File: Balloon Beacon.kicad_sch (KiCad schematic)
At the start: 52 parts, among them J1 PV Input, J2 Serial, J3 ICSP, J4 I2C, J6 GPS_ANT, Q1 AO3401A, U1 CJ431, U2 ATmega328PB-MU, U3 STC22K33048-26.000MT, U4 LM50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

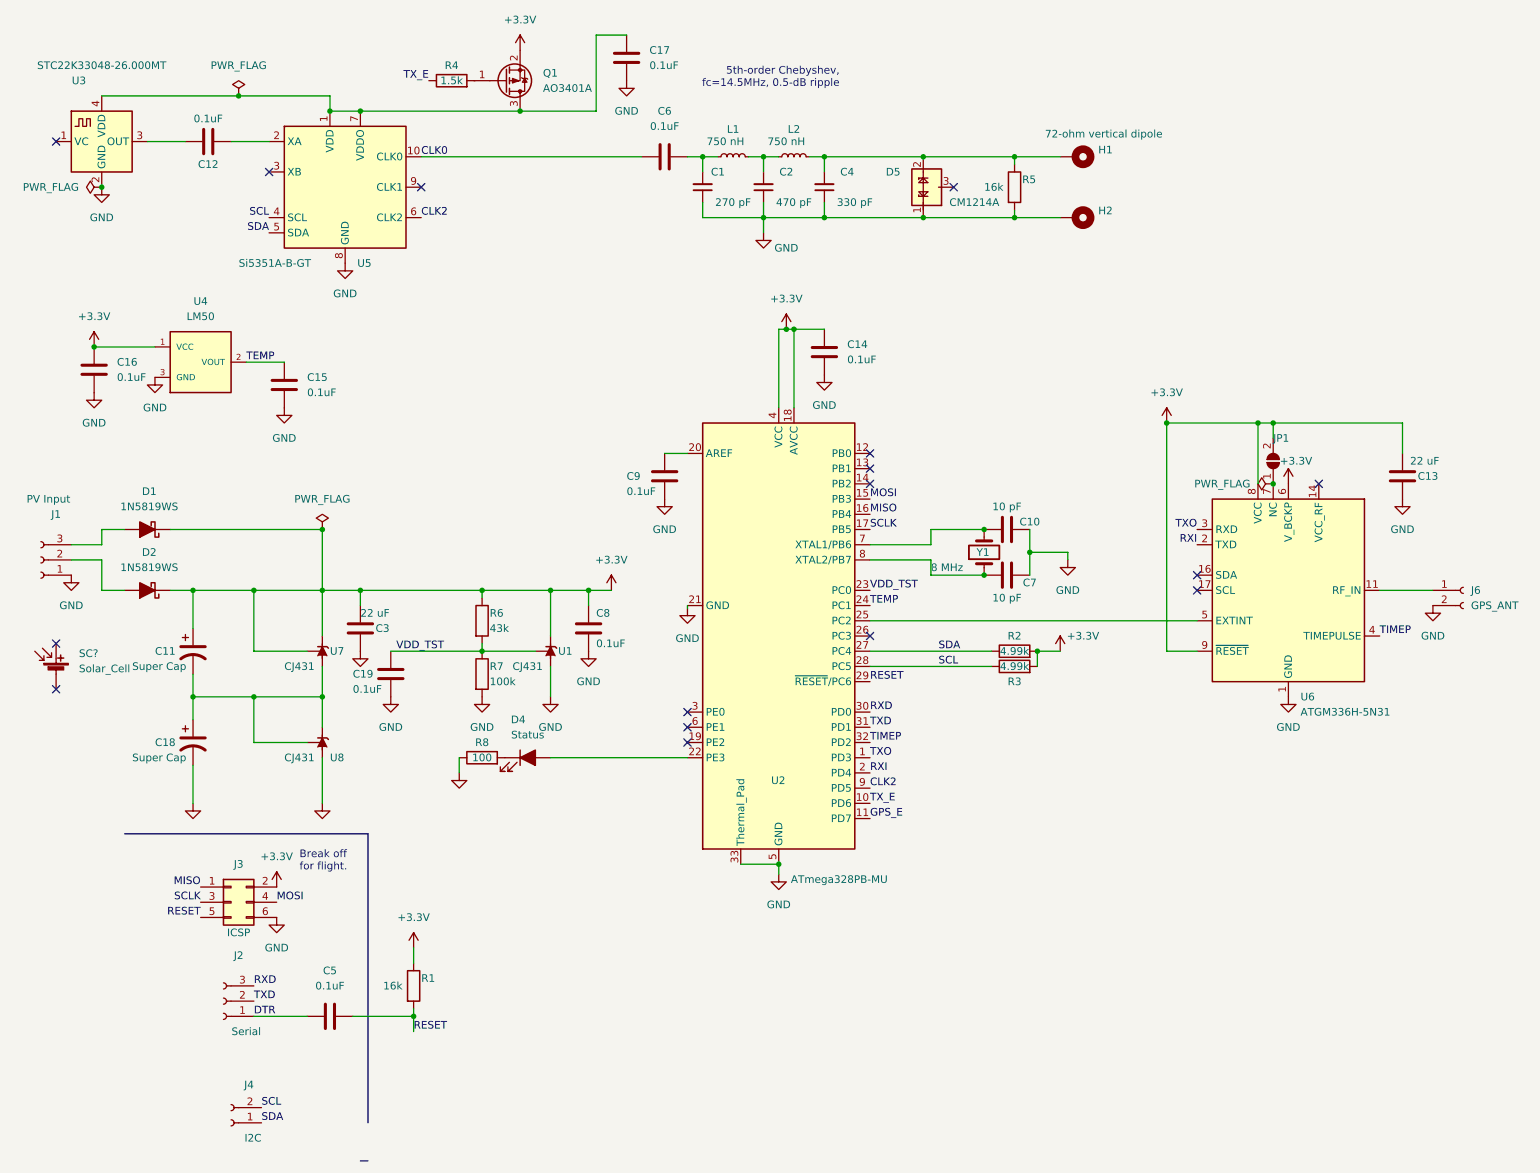
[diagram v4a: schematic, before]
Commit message: Changed TCXO to an available one.
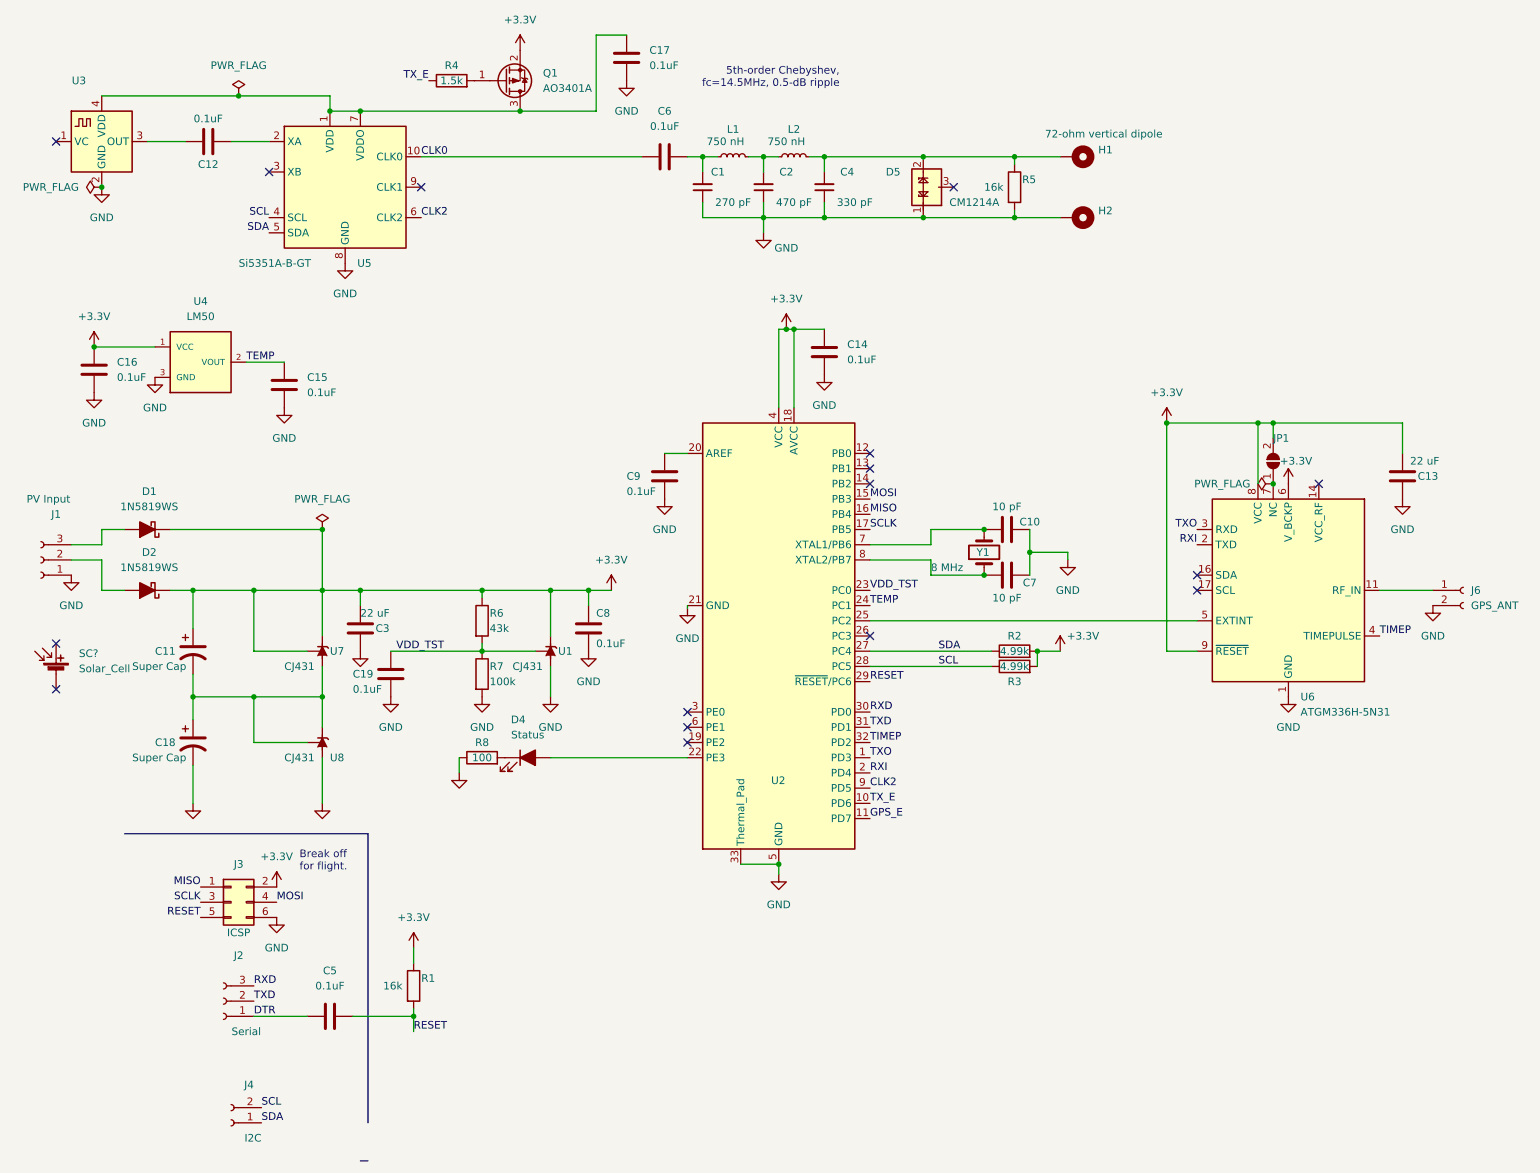
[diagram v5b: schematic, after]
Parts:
- U2: value ATmega328PB-MU -> (none); footprint Package_DFN_QFN:QFN-32-1EP_5x5mm_P0.5mm_EP3.3x3.3mm -> (none); LCSC C967933 -> (none)
- U3: value STC22K33048-26.000MT -> (none); footprint Oscillator:Oscillator_SMD_Fox_FT5H_5.0x3.2mm -> (none)
- U6: LCSC (none) -> C90770
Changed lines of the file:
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@@
       (effects (font (size 1.27 1.27)) (justify left))
     )
-    (property "Value" "ATmega328PB-MU" (id 1) (at 142.9894 157.48 0)
-      (effects (font (size 1.27 1.27)) (justify left))
-    )
-    (property "Footprint" "Package_DFN_QFN:QFN-32-1EP_5x5mm_P0.5mm_EP3.3x3.3mm" (id 2) (at 140.97 116.84 0)
+    (property "Value" "" (id 1) (at 142.9894 157.48 0)
+      (effects (font (size 1.27 1.27)) (justify left))
+    )
+    (property "Footprint" "" (id 2) (at 140.97 116.84 0)
       (effects (font (size 1.27 1.27) italic) hide)
     )
     (property "Datasheet" "http://ww1.microchip.com/downloads/en/DeviceDoc/40001906C.pdf" (id 3) (at 140.97 116.84 0)
-      (effects (font (size 1.27 1.27)) hide)
-    )
-    (property "LCSC" "C967933" (id 4) (at 140.97 116.84 0)
       (effects (font (size 1.27 1.27)) hide)
     )
@@
       (effects (font (size 1.27 1.27)) hide)
     )
+    (property "LCSC" "C90770" (id 4) (at 226.06 109.22 0)
+      (effects (font (size 1.27 1.27)) hide)
+    )
     (pin "1")
     (pin "10")
@@
     (in_bom yes) (on_board yes)
     (property "Reference" "U3" (id 0) (at 24.13 24.13 0))
-    (property "Value" "STC22K33048-26.000MT" (id 1) (at 27.94 21.59 0))
-    (property "Footprint" "Oscillator:Oscillator_SMD_Fox_FT5H_5.0x3.2mm" (id 2) (at 27.94 53.34 0)
-      (effects (font (size 1.27 1.27)) hide)
-    )
-    (property "Datasheet" "https://suntsu.com/wp-content/uploads/2019/07/STC22K-Series.pdf" (id 3) (at 27.94 34.29 0)
+    (property "Value" "" (id 1) (at 27.94 21.59 0))
+    (property "Footprint" "" (id 2) (at 27.94 53.34 0)
+      (effects (font (size 1.27 1.27)) hide)
+    )
+    (property "Datasheet" "https://www.taitien.com/wp-content/uploads/2015/12/XO-0076_TX.pdf" (id 3) (at 27.94 34.29 0)
       (effects (font (size 1.27 1.27)) hide)
     )
@@
     )
     (path "/ea8a827f-ae0c-4cf1-8927-35f036a4c0c6"
-      (reference "U3") (unit 1) (value "STC22K33048-26.000MT") (footprint "Oscillator:Oscillator_SMD_Fox_FT5H_5.0x3.2mm")
+      (reference "U3") (unit 1) (value "TXEABLSANF-24.000000") (footprint "Oscillator:Oscillator_SMD_EuroQuartz_XO32-4Pin_3.2x2.5mm_HandSoldering")
     )
     (path "/56d74f4a-c28a-4ee6-9f0c-d886e3d08c1f"

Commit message: Deleted a solar cell on the schematic.
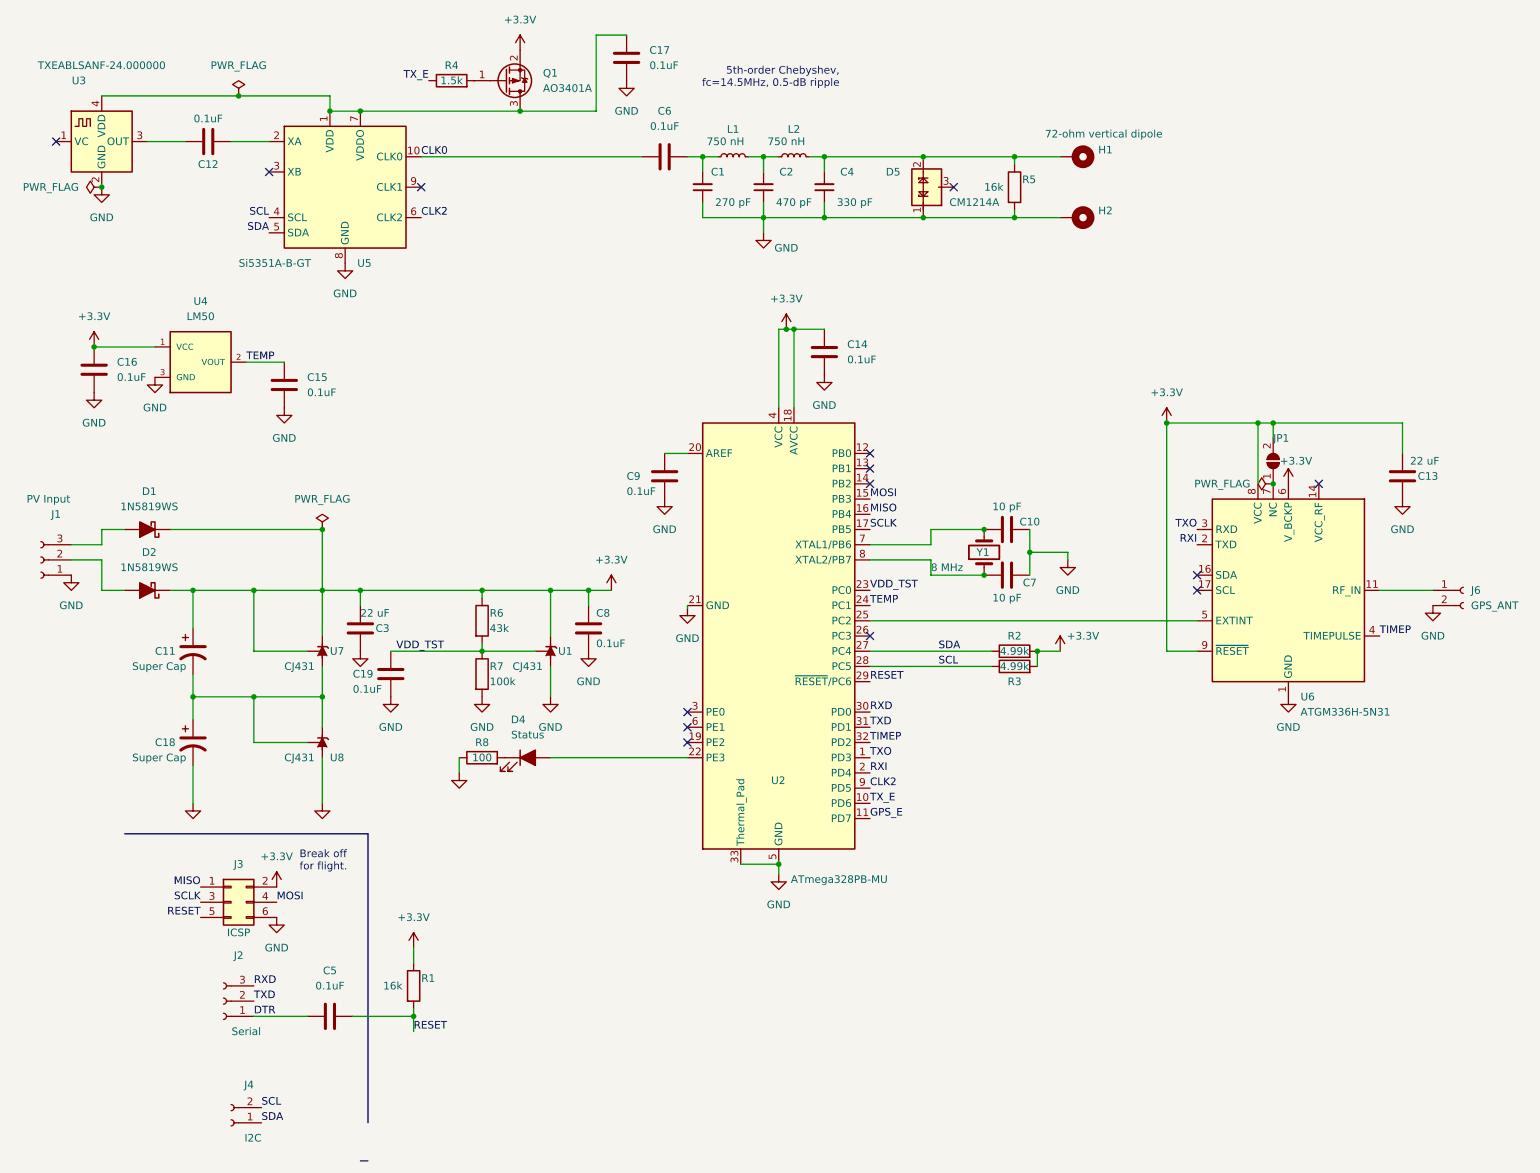
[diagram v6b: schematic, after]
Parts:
- removed SC?: Solar_Cell, symbol Device:Solar_Cell
- U2: value (none) -> ATmega328PB-MU; footprint (none) -> Package_DFN_QFN:QFN-32-1EP_5x5mm_P0.5mm_EP3.3x3.3mm
- U3: value (none) -> TXEABLSANF-24.000000; footprint (none) -> Oscillator:Oscillator_SMD_EuroQuartz_XO32-4Pin_3.2x2.5mm_HandSoldering
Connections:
- no-connect marks 16 -> 14
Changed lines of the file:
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@@
   (no_connect (at 210.82 106.68))
   (no_connect (at 210.82 109.22))
-  (no_connect (at 20.32 118.11))
-  (no_connect (at 20.32 125.73))
   (no_connect (at 156.21 86.36))
   (no_connect (at 156.21 88.9))
@@
       (effects (font (size 1.27 1.27)) (justify left))
     )
-    (property "Value" "" (id 1) (at 142.9894 157.48 0)
-      (effects (font (size 1.27 1.27)) (justify left))
-    )
-    (property "Footprint" "" (id 2) (at 140.97 116.84 0)
+    (property "Value" "ATmega328PB-MU" (id 1) (at 142.9894 157.48 0)
+      (effects (font (size 1.27 1.27)) (justify left))
+    )
+    (property "Footprint" "Package_DFN_QFN:QFN-32-1EP_5x5mm_P0.5mm_EP3.3x3.3mm" (id 2) (at 140.97 116.84 0)
       (effects (font (size 1.27 1.27) italic) hide)
     )
@@
     (pin "1")
   )
-  (symbol (lib_id "Device:Solar_Cell") (at 20.32 123.19 0) (unit 1)
-    (in_bom yes) (on_board yes) (fields_autoplaced)
-    (property "Reference" "SC?" (id 0) (at 24.13 119.7609 0)
-      (effects (font (size 1.27 1.27)) (justify left))
-    )
-    (property "Value" "Solar_Cell" (id 1) (at 24.13 122.3009 0)
-      (effects (font (size 1.27 1.27)) (justify left))
-    )
-    (property "Footprint" "" (id 2) (at 20.32 121.666 90)
-      (effects (font (size 1.27 1.27)) hide)
-    )
-    (property "Datasheet" "https://www.mouser.com/ProductDetail/PowerFilm/MPT36-75?qs=BJlw7L4Cy79PADpX3LN7rA%3D%3D" (id 3) (at 20.32 121.666 90)
-      (effects (font (size 1.27 1.27)) hide)
-    )
-    (pin "1")
-    (pin "2")
-  )
   (symbol (lib_id "Device:C") (at 45.72 34.29 270) (unit 1)
     (in_bom yes) (on_board yes)
@@
     (in_bom yes) (on_board yes)
     (property "Reference" "U3" (id 0) (at 24.13 24.13 0))
-    (property "Value" "" (id 1) (at 27.94 21.59 0))
-    (property "Footprint" "" (id 2) (at 27.94 53.34 0)
+    (property "Value" "TXEABLSANF-24.000000" (id 1) (at 27.94 21.59 0))
+    (property "Footprint" "Oscillator:Oscillator_SMD_EuroQuartz_XO32-4Pin_3.2x2.5mm_HandSoldering" (id 2) (at 27.94 53.34 0)
       (effects (font (size 1.27 1.27)) hide)
     )
@@
       (reference "R8") (unit 1) (value "100") (footprint "Resistor_SMD:R_0603_1608Metric_Pad0.98x0.95mm_HandSolder")
     )
-    (path "/636dce35-ff98-43a1-aeb4-4c95a15832a9"
-      (reference "SC?") (unit 1) (value "Solar_Cell") (footprint "")
-    )
     (path "/02163717-eac1-4757-bdb2-c94f527ed6dd"
